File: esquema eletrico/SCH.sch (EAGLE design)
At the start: 11 parts, among them IC1 ULN2003AN, U1 ARDUINOR3-DIMENSION

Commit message: esquemático para dois motores
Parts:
- added IC2: ULN2003AN, uln-udn:ULN2003AN
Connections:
- removed net FIO_AMARELO: IC1.O3
- removed net FIO_AZUL: IC1.O1
- removed net FIO_LARANJA: IC1.O4
- removed net FIO_ROSA: IC1.O2
- removed net FIO_VERMELHO: IC1.O5
- new net D12: IC1.I3, IC2.I3, U1.D12
- new net D13: IC1.I4, IC2.I4, U1.D13
- new net D7: U1.D7
- new net FIO_AMA: IC1.O3, IC2.O3
- new net FIO_AZU: IC1.O1, IC2.O1
- new net FIO_LAR: IC1.O4, IC2.O4
- new net FIO_ROS: IC1.O2, IC2.O2
- new net FIO_VER: IC1.O5, IC2.O5
- net 5V_EXTERNO: now also IC2.CD+
- net D10: now also IC1.I1, IC2.I1; no longer IC1.I3
- net D11: now also IC1.I2, IC2.I2; no longer IC1.I4
- net D5: no longer U1.D5
- net D8: no longer IC1.I1
- net D9: no longer IC1.I2
- net GND: now also IC2.GND
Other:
- note added: "Motor M1O"
- note added: "Motor M2C"
- note removed: "Motor"
- moved on the sheet: IC1

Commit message: Sch atualizado
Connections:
- removed net D12: IC1.I3, IC2.I3, U1.D12
- removed net D13: IC1.I4, IC2.I4, U1.D13
- new net D2: C1.2, CFC_1.P, R4.2
- new net D3: C2.2, CFC_2.P, R3.2
- new net D4: IC1.I1, U1.D4
- net D10: now also IC2.I3; no longer IC1.I1, IC2.I1
- net D11: now also IC2.I4; no longer IC1.I2, IC2.I2
- net D5: now also IC1.I2, U1.D5; no longer C1.2, CFC_1.P, R4.2
- net D6: now also IC1.I3; no longer C2.2, CFC_2.P, R3.2
- net D7: now also IC1.I4
- net D8: now also IC2.I1
- net D9: now also IC2.I2
- net GND: now also U1.D12, U1.D13

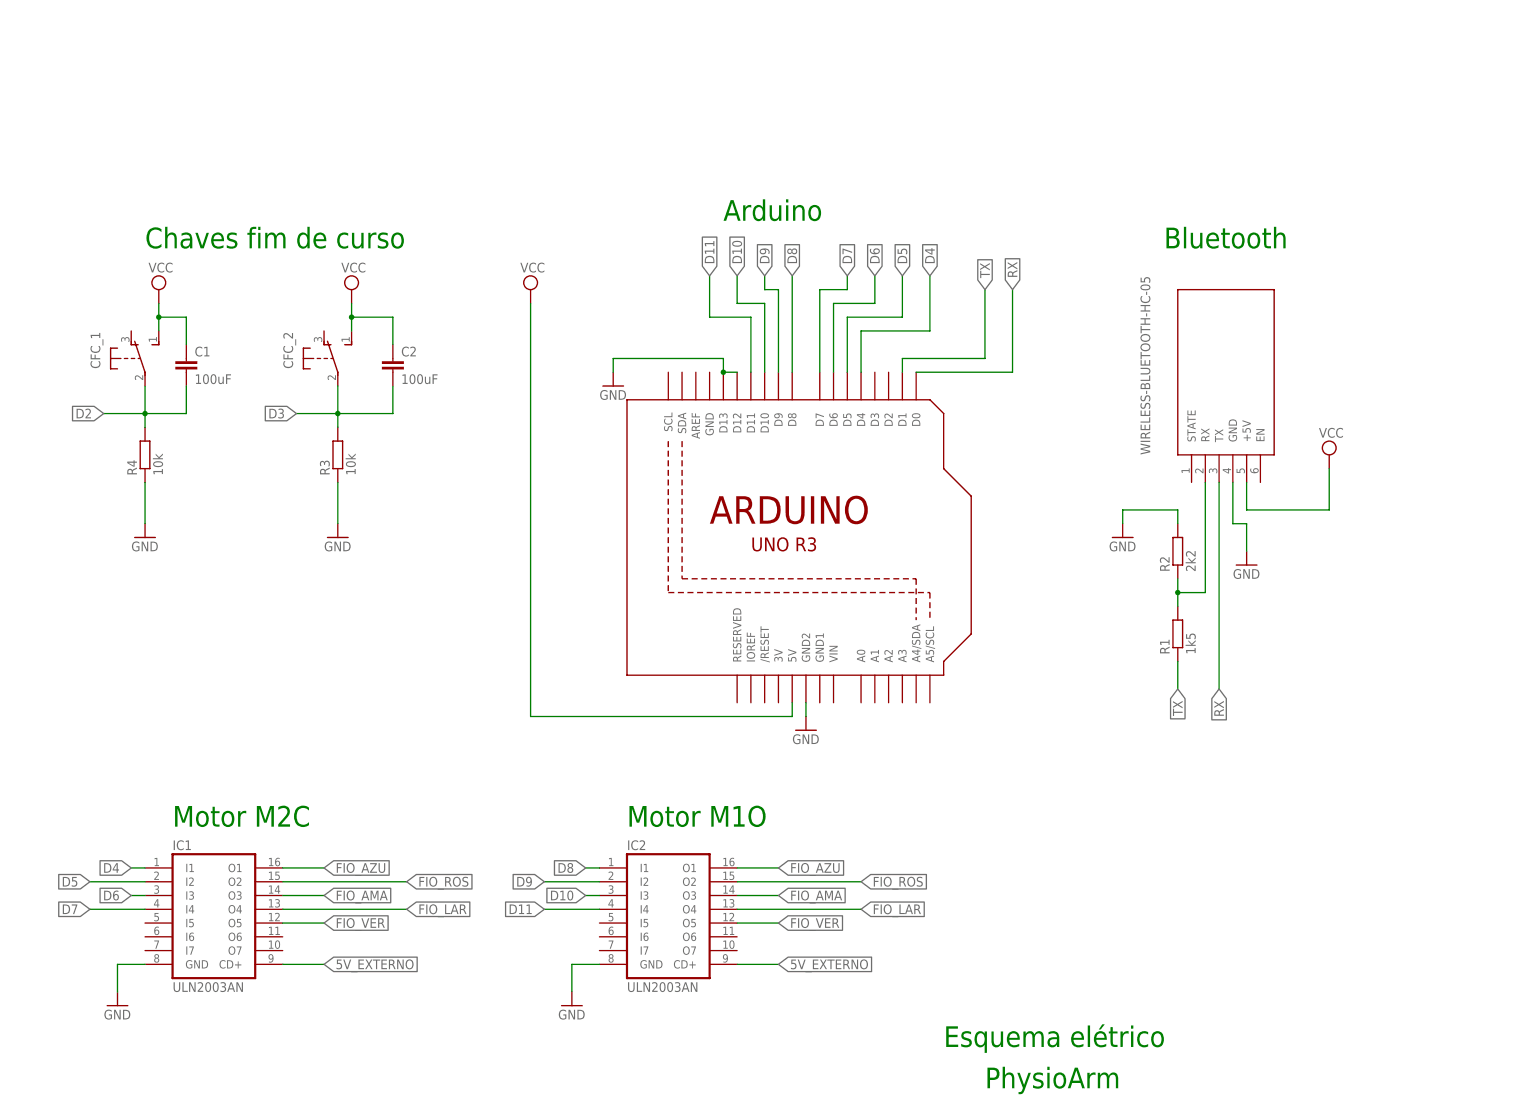
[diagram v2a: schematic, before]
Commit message: esquemático final dos testes
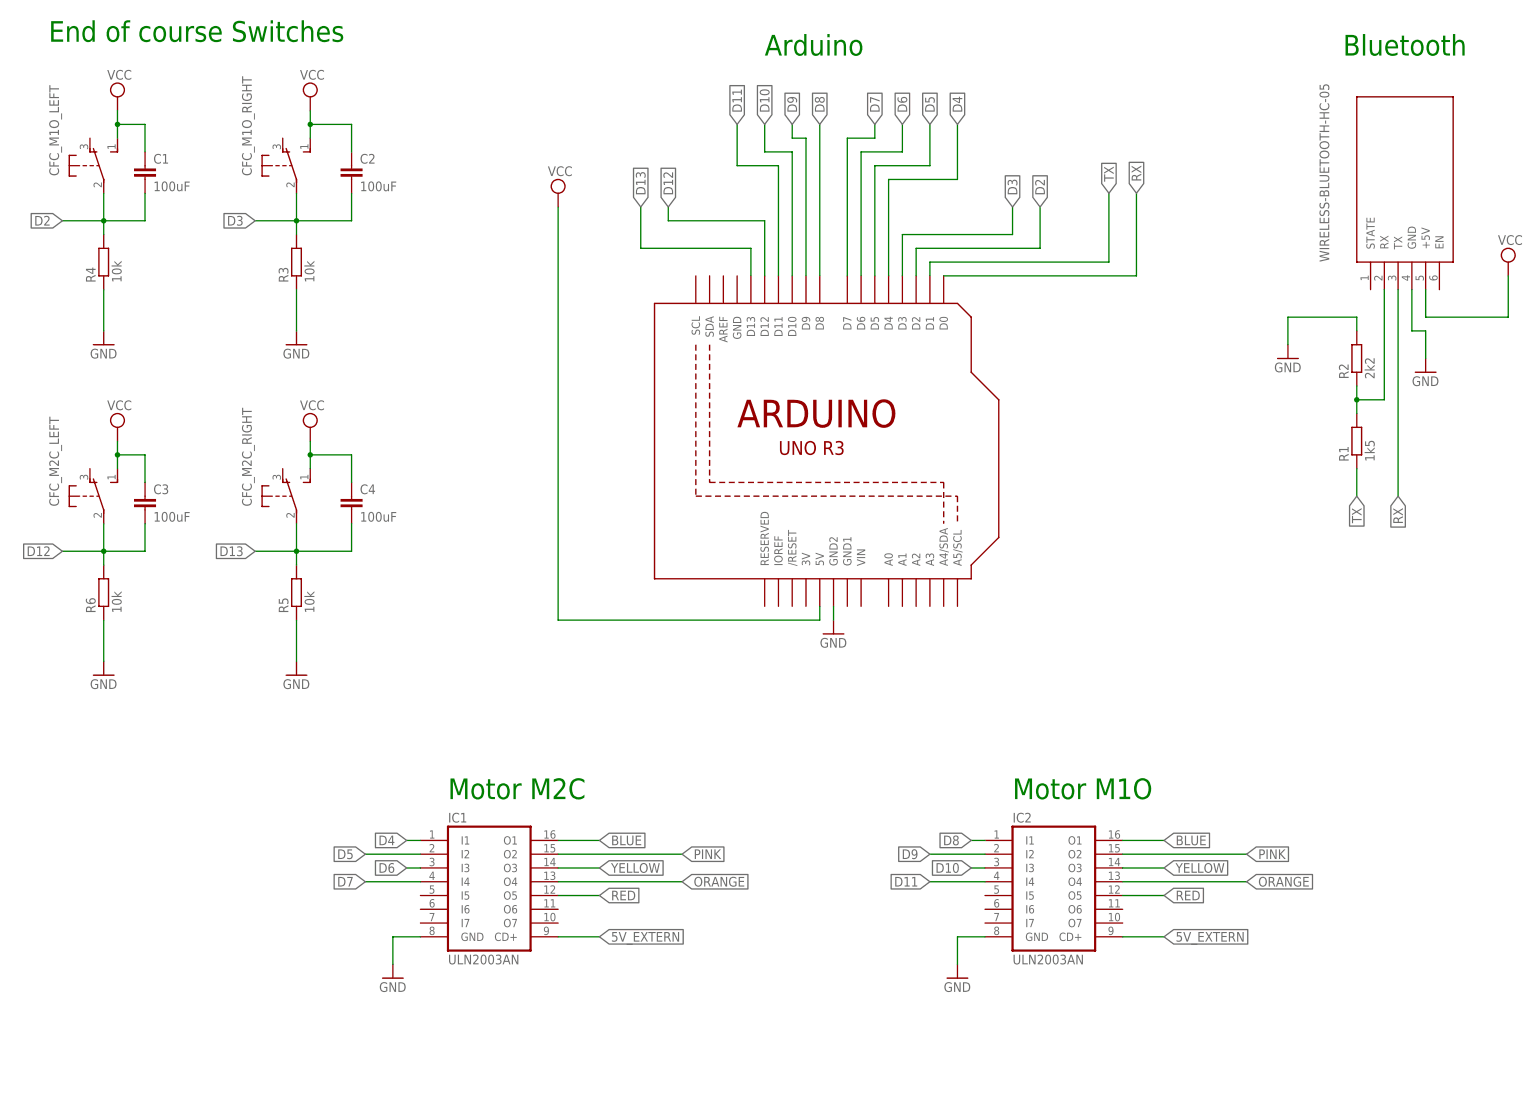
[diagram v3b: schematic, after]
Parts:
- removed CFC_1, CFC_2: 9450-1, switch-misc:9450-1
- added C3, C4: 100uF, capacitor-wima:C2,5-3
- added CFC_M1O_LEFT, CFC_M1O_RIGHT, CFC_M2C_LEFT, CFC_M2C_RIGHT: 9450-1, switch-misc:9450-1
- added R5, R6: 10k, resistor:R-EU_0204/5
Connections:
- net 5V_EXTERNO renamed 5V_EXTERN
- net FIO_AMA renamed YELLOW
- net FIO_AZU renamed BLUE
- net FIO_LAR renamed ORANGE
- net FIO_ROS renamed PINK
- net FIO_VER renamed RED
- new net D12: C3.2, CFC_M2C_LEFT.P, R6.2, U1.D12
- new net D13: C4.2, CFC_M2C_RIGHT.P, R5.2, U1.D13
- net D2: now also CFC_M1O_LEFT.P, U1.D2; no longer CFC_1.P
- net D3: now also CFC_M1O_RIGHT.P, U1.D3; no longer CFC_2.P
- net GND: now also R5.1, R6.1; no longer U1.D12, U1.D13
- net VCC: now also C3.1, C4.1, CFC_M1O_LEFT.S, CFC_M1O_RIGHT.S, CFC_M2C_LEFT.S, CFC_M2C_RIGHT.S; no longer CFC_1.S, CFC_2.S
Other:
- note added: "End of course Switches"
- note removed: "Chaves fim de curso"
- note removed: "Esquema elétrico"
- note removed: "PhysioArm"
- moved on the sheet: C1, C2, IC1, IC2, R1, R2, R3, R4, WIRELESS-BLUETOOTH-HC-05
